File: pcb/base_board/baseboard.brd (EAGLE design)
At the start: 88 x 85 mm, 38 parts, among them IC1 LD117AS33TR, SW1 324_SW, SW2 324_SW, SW20 324_SW, SW3 324_SW, SW4 324_SW, U5 CH340C

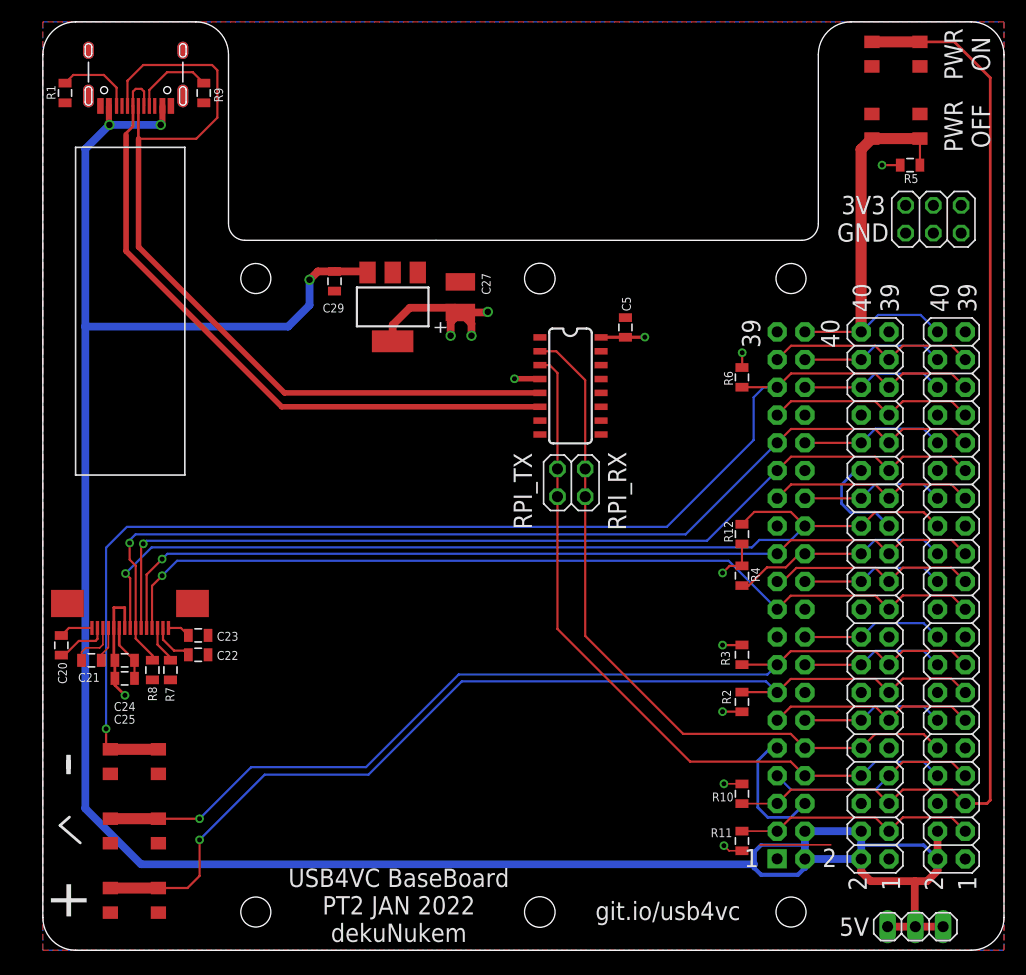
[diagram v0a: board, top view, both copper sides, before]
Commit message: updated PCB for second prototype run
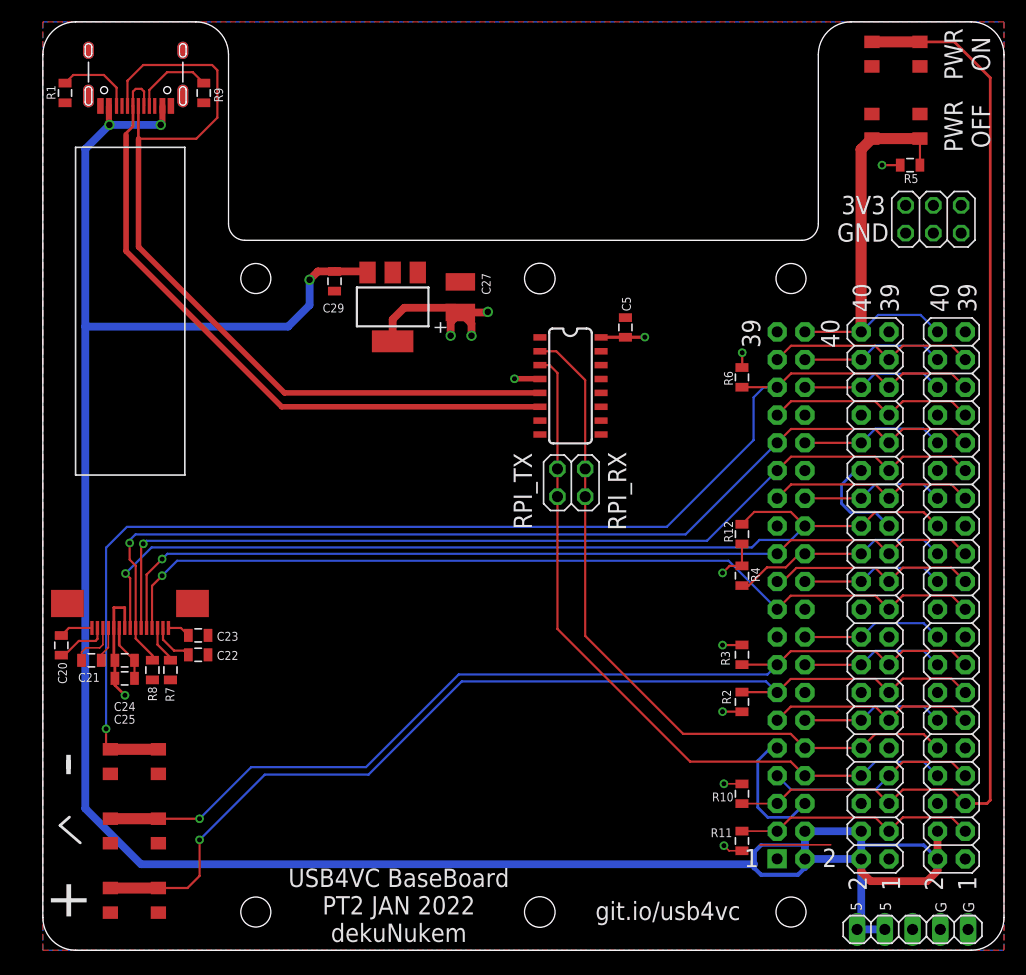
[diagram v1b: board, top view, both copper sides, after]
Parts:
- JP5: device pinhead:1X03 -> pinhead:1X05
- moved JP5 0.36 mm to (79.6, 1.91)
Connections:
- net +5V: no longer JP5.3
- net GND: now also JP5.4, JP5.5
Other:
- outline, holes or cut-outs redrawn
- board text added: "5"
- board text added: "G"
- board text removed: "5V"
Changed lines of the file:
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@@
 <wire x1="17" y1="82" x2="17" y2="66.5" width="0" layer="20"/>
 <wire x1="17" y1="66.5" x2="18.5" y2="65" width="0" layer="20" curve="90"/>
-<wire x1="18.5" y1="65" x2="36" y2="65" width="0" layer="20"/>
-<wire x1="36" y1="65" x2="69.5" y2="65" width="0" layer="20"/>
+<wire x1="18.5" y1="65" x2="69.5" y2="65" width="0" layer="20"/>
 <wire x1="69.5" y1="65" x2="71" y2="66.5" width="0" layer="20" curve="90"/>
 <wire x1="71" y1="66.5" x2="71" y2="82" width="0" layer="20"/>
@@
 <text x="75.1332" y="68.2244" size="1.6764" layer="25" rot="R180" align="center">3V3</text>
 <text x="75.0824" y="65.7098" size="1.6764" layer="25" rot="R180" align="center">GND</text>
-<text x="72.9234" y="1.3208" size="1.6764" layer="25">5V</text>
+<text x="76.6318" y="4.4196" size="1.016" layer="25" rot="R270">5</text>
 <text x="85.471" y="5.461" size="1.6764" layer="25" rot="R90">1</text>
 <text x="82.423" y="5.461" size="1.6764" layer="25" rot="R90">2</text>
@@
 <rectangle x1="50.8" y1="0" x2="71.628" y2="8.128" layer="41"/>
 <rectangle x1="50.8" y1="0" x2="71.628" y2="8.128" layer="42"/>
+<text x="73.9648" y="4.4196" size="1.016" layer="25" rot="R270">5</text>
+<text x="81.7118" y="4.4196" size="1.016" layer="25" rot="R270">G</text>
+<text x="84.2518" y="4.4196" size="1.016" layer="25" rot="R270">G</text>
 </plain>
 <attributes>
@@
 <attribute name="NAME" x="62.9031" y="26.0604" size="0.8128" layer="25" rot="R90"/>
 </element>
-<element name="JP5" library="pinhead" library_urn="urn:adsk.eagle:library:325" package="1X03" package3d_urn="urn:adsk.eagle:package:22458/2" value="" x="79.883" y="2.159" smashed="yes">
-<attribute name="POPULARITY" value="92" x="79.883" y="2.159" size="0.8128" layer="27" display="off"/>
-<attribute name="VALUE" x="76.073" y="-1.016" size="1.27" layer="27"/>
+<element name="JP5" library="pinhead" library_urn="urn:adsk.eagle:library:325" package="1X05" package3d_urn="urn:adsk.eagle:package:22469/2" value="" x="79.629" y="1.905" smashed="yes">
+<attribute name="POPULARITY" value="69" x="79.629" y="1.905" size="0.8128" layer="27" display="off"/>
+<attribute name="VALUE" x="75.819" y="-1.27" size="1.27" layer="27"/>
 </element>
 <element name="SW2" library="3pos_slide_switch_centered" package="342_SWICH_FOOT" value="324_SW" x="78.105" y="82.042" smashed="yes"/>
@@
 <contactref element="JP6" pad="5"/>
 <wire x1="72.136" y1="9.652" x2="65.659" y2="9.652" width="0.1524" layer="1"/>
+<contactref element="JP5" pad="5"/>
+<contactref element="JP5" pad="4"/>
 </signal>
 <signal name="+3V3">
@@
 <wire x1="62.23" y1="27.94" x2="63.997" y2="27.94" width="0.2032" layer="1"/>
 <wire x1="63.997" y1="27.94" x2="64.008" y2="27.951" width="0.2032" layer="1"/>
-<wire x1="32.0294" y1="55.7526" x2="32.0294" y2="57.2512" width="0.7112" layer="1"/>
-<wire x1="33.6016" y1="58.8234" x2="32.0294" y2="57.2512" width="0.7112" layer="1"/>
-<wire x1="37.7952" y1="58.8234" x2="33.6016" y2="58.8234" width="0.7112" layer="1"/>
+<wire x1="32.0294" y1="55.7526" x2="32.0294" y2="57.7592" width="0.7112" layer="1"/>
+<wire x1="33.0936" y1="58.8234" x2="32.0294" y2="57.7592" width="0.7112" layer="1"/>
+<wire x1="37.7952" y1="58.8234" x2="33.0936" y2="58.8234" width="0.7112" layer="1"/>
 <wire x1="37.7952" y1="58.8234" x2="38.227" y2="58.3916" width="0.7112" layer="1"/>
 <wire x1="38.227" y1="58.3916" x2="37.338" y2="57.5026" width="0.7112" layer="1"/>
@@
 <wire x1="74.93" y1="8.3566" x2="74.93" y2="7.1882" width="0.7112" layer="1"/>
 <wire x1="74.93" y1="7.1882" x2="75.7936" y2="6.3246" width="0.7112" layer="1"/>
-<wire x1="75.7936" y1="6.3246" x2="79.8322" y2="6.3246" width="0.7112" layer="1"/>
-<wire x1="79.8322" y1="6.3246" x2="80.9498" y2="6.3246" width="0.7112" layer="1"/>
+<wire x1="75.7936" y1="6.3246" x2="80.9498" y2="6.3246" width="0.7112" layer="1"/>
 <wire x1="81.915" y1="7.2898" x2="81.915" y2="8.3566" width="0.7112" layer="1"/>
 <wire x1="80.9498" y1="6.3246" x2="81.915" y2="7.2898" width="0.7112" layer="1"/>
@@
 <wire x1="25.1816" y1="62.1504" x2="24.4196" y2="61.3884" width="0.7112" layer="1"/>
 <wire x1="26.7056" y1="62.1504" x2="29.6316" y2="62.1504" width="0.7112" layer="1"/>
-<contactref element="JP5" pad="1"/>
-<contactref element="JP5" pad="2"/>
-<contactref element="JP5" pad="3"/>
-<wire x1="79.8322" y1="6.3246" x2="79.8322" y2="2.2098" width="0.7112" layer="1"/>
-<wire x1="79.8322" y1="2.2098" x2="79.883" y2="2.159" width="0.7112" layer="1"/>
-<wire x1="77.343" y1="2.159" x2="79.7814" y2="2.159" width="0.7112" layer="1"/>
-<wire x1="79.7814" y1="2.159" x2="79.8322" y2="2.2098" width="0.7112" layer="1"/>
-<wire x1="79.883" y1="2.159" x2="82.423" y2="2.159" width="0.7112" layer="1"/>
 <wire x1="69.7718" y1="10.8966" x2="74.93" y2="10.8966" width="0.7112" layer="16"/>
 <wire x1="3.8862" y1="73.3552" x2="3.8862" y2="57.0992" width="0.7112" layer="16"/>
@@
 <wire x1="3.8862" y1="12.9794" x2="8.9916" y2="7.874" width="0.7112" layer="16"/>
 <wire x1="3.8862" y1="57.0992" x2="22.4536" y2="57.0992" width="0.7112" layer="16"/>
+<contactref element="JP5" pad="2"/>
+<contactref element="JP5" pad="1"/>
+<wire x1="74.93" y1="8.3566" x2="74.93" y2="2.286" width="0.7112" layer="16"/>
+<wire x1="74.93" y1="2.286" x2="74.549" y2="1.905" width="0.7112" layer="16"/>
+<wire x1="77.089" y1="1.905" x2="74.549" y2="1.905" width="0.7112" layer="16"/>
 </signal>
 <signal name="N$2">

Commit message: added gerber file
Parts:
- removed C25: 1uF, clock:0805
- added JP3: (no value), adafruit_changed:1X01
- moved C22 0.57 mm to (14.5, 26.5)
- moved JP6 0.28 mm to (81.3, 67.1)
- moved C23 0.28 mm to (14.5, 28.7)
- moved R7 0.25 mm to (11.9, 25.7)
- moved C21 0.13 mm to (4.32, 26.5)
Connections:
- net +3V3: no longer C25.2
- net GND: no longer C25.1
- net N$32: now also JP3.1
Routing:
- net PLUS_BUTTON: track 93.8 -> 91.9 mm
- net +3V3: track 48.2 -> 46.4 mm
- net GND: track 32.7 -> 31.0 mm
- net N$40: track 3.96 -> 4.58 mm
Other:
- board text added: "3"
- board text added: "RST"
- board text removed: "3V3"
- board text removed: "GND"

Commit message: updated component values
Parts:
- C29: value 10uF -> 2.2uF
- R2, R3, R5, R6: value 390K -> 5.1K
- R8: value 12K -> 5.1K
- renumbered JP1 to P2, JP2 to P3, PCB1 to P1
